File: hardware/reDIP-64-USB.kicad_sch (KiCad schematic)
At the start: 35 parts, among them J1 USB_C_Receptacle, Q1 PDTA143ZMB, U10 PTN5110, U11 FUSB340, U12 DSC1103CE2-135.0000, U13 FSA2259, U8 LFE5UM5G-25F-8MG285C

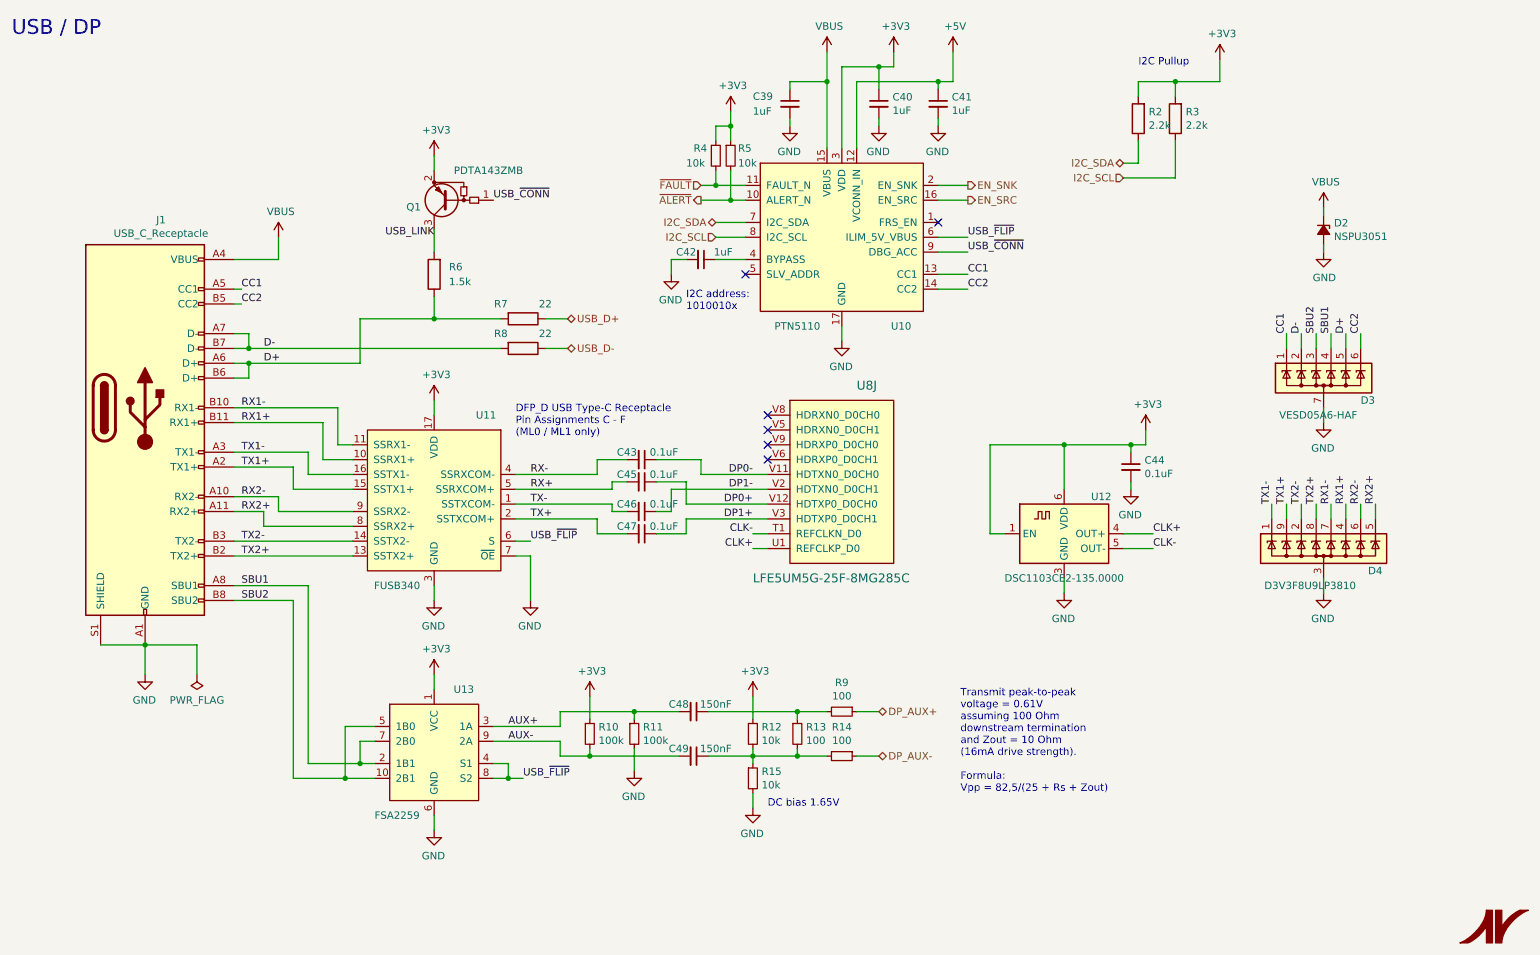
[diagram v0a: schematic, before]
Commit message: Various improvements
* Removed slash from sheet names
* Reannotated schematics
* Example derivation of clocks in schematics
* Identical capacitors for DisplayPort main lanes and AUX
* Replaced switch FSA2259UMX with FSUSB42UMX
* Modified PCB physical stackup to (hopefully) be manufacturable
* Only one microvia size (0.1mm)
* Changed track width for differential pairs
* Routing cleanups and improvements
* Added files for manufacture
* Updated README

Many thanks for advice and help go to @azonenberg, @DX-MON, @gatecat,
@smunaut, and @zyp.
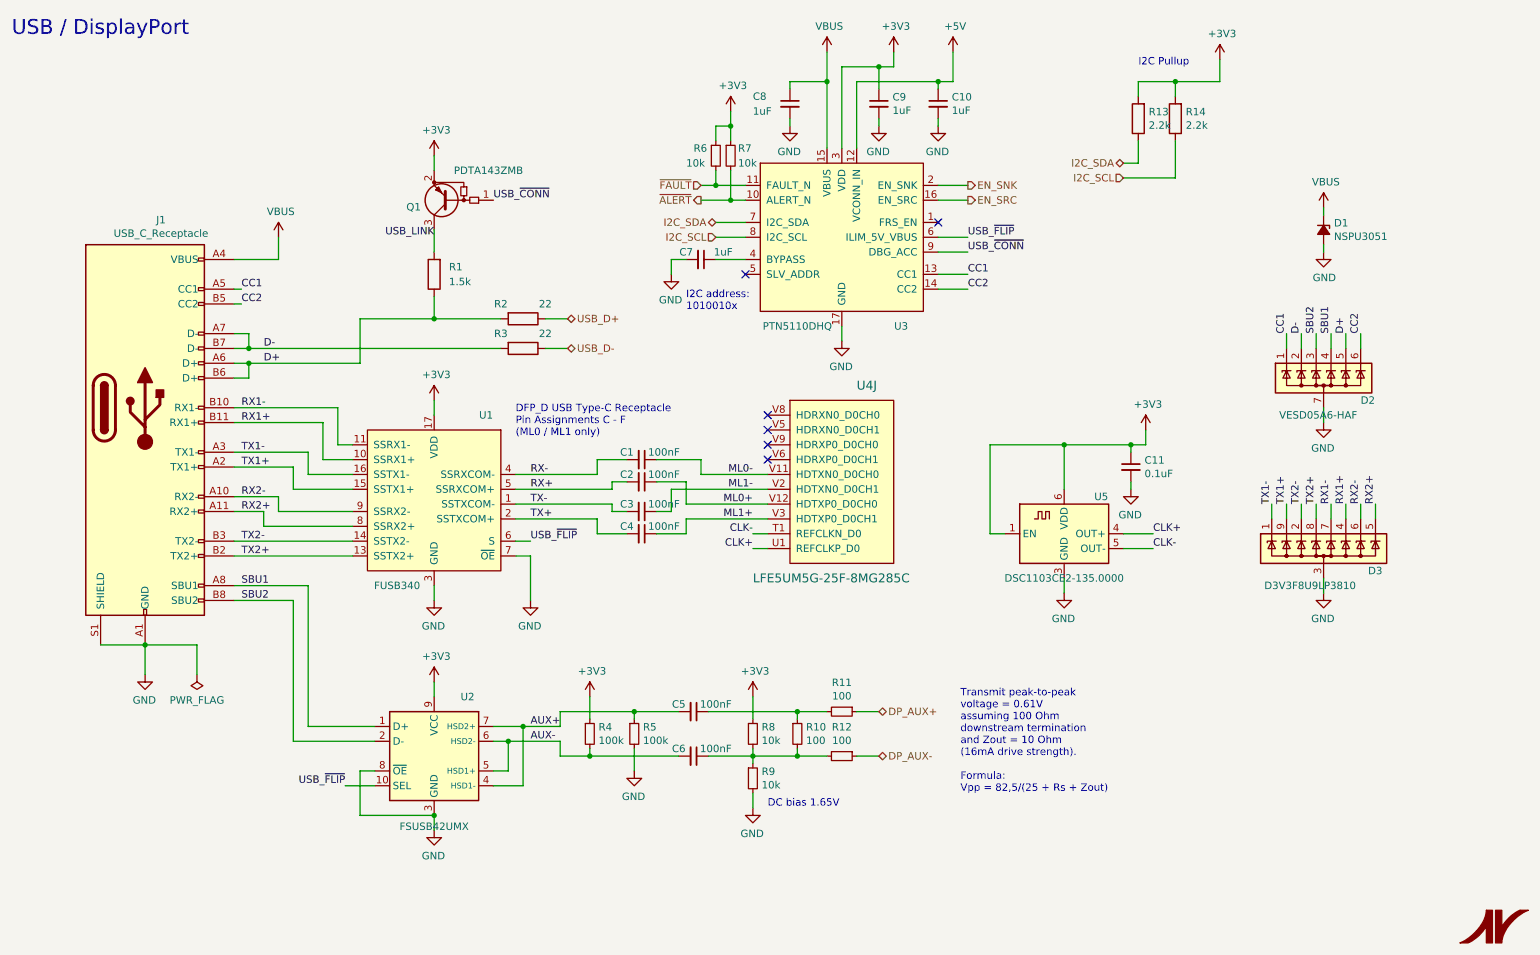
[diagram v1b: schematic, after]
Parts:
- removed U13: FSA2259, ONSemi:CASE523BC_1.4x1.8_P0.4mm, symbol ONSemi:FSA2259
- added U2: FSUSB42UMX, ONSemi:CASE523BC_1.4x1.8_P0.4mm, symbol ONSemi:FSUSB42UMX
- C1: renamed from C43; value 0.1uF -> 100nF; Notes 1.2V DC DERATED TO 0.1uF -> (none)
- C2: renamed from C45; value 0.1uF -> 100nF; Notes 1.2V DC DERATED TO 0.1uF -> (none)
- C3: renamed from C46; value 0.1uF -> 100nF; Notes 1.2V DC DERATED TO 0.1uF -> (none)
- C4: renamed from C47; value 0.1uF -> 100nF; Notes 1.2V DC DERATED TO 0.1uF -> (none)
- C5: renamed from C48; value 150nF -> 100nF; Notes 1.65V DC DERATED TO 150nF -> (none); PN GRM033R60J224ME15D -> GRM033R60J224KE15D
- C6: renamed from C49; value 150nF -> 100nF; Notes 1.65V DC DERATED TO 150nF -> (none); PN GRM033R60J224ME15D -> GRM033R60J224KE15D
- U3: renamed from U10; value PTN5110 -> PTN5110DHQ
- renumbered C41 to C10, C44 to C11, C42 to C7, C39 to C8, C40 to C9, D2 to D1, D3 to D2, D4 to D3, R6 to R1, R13 to R10, R9 to R11, R14 to R12, R2 to R13, R3 to R14, R7 to R2, R8 to R3, R10 to R4, R11 to R5, R4 to R6, R5 to R7, R12 to R8, R15 to R9, U11 to U1, U8 to U4, U12 to U5
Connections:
- net +3V3: now also U2.9 (VCC)
- net AUX+: now also U2.4 (HSD1-), U2.7 (HSD2+)
- net AUX-: now also U2.5 (HSD1+), U2.6 (HSD2-)
- net GND: now also U2.3 (GND), U2.8 (~OE)
- net SBU1: now also U2.1 (D+)
- net SBU2: now also U2.2 (D-)
- net USB_~FLIP~: now also U2.10 (SEL)
- net DP0+ renamed ML0+
- net DP0- renamed ML0-
- net DP1+ renamed ML1+
- net DP1- renamed ML1-
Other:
- note added: "USB / DisplayPort"
- note removed: "USB / DP"

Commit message: Corrected BOM for C1-C6
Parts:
- C1, C2, C3, C4, C5, C6: PN GRM033R60J224KE15D -> GRM033R60J104KE19D
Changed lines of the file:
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@@
       (effects (font (size 1.27 1.27)) hide)
     )
-    (property "PN" "GRM033R60J224KE15D" (id 6) (at 130.81 97.79 0)
+    (property "PN" "GRM033R60J104KE19D" (id 6) (at 130.81 97.79 0)
       (effects (font (size 1.27 1.27)) hide)
     )
@@
       (effects (font (size 1.27 1.27)) hide)
     )
-    (property "PN" "GRM033R60J224KE15D" (id 6) (at 130.81 101.6 0)
+    (property "PN" "GRM033R60J104KE19D" (id 6) (at 130.81 101.6 0)
       (effects (font (size 1.27 1.27)) hide)
     )
@@
       (effects (font (size 1.27 1.27)) hide)
     )
-    (property "PN" "GRM033R60J224KE15D" (id 6) (at 130.81 106.68 0)
+    (property "PN" "GRM033R60J104KE19D" (id 6) (at 130.81 106.68 0)
       (effects (font (size 1.27 1.27)) hide)
     )
@@
       (effects (font (size 1.27 1.27)) hide)
     )
-    (property "PN" "GRM033R60J224KE15D" (id 6) (at 130.81 110.49 0)
+    (property "PN" "GRM033R60J104KE19D" (id 6) (at 130.81 110.49 0)
       (effects (font (size 1.27 1.27)) hide)
     )
@@
       (effects (font (size 1.27 1.27)) hide)
     )
-    (property "PN" "GRM033R60J224KE15D" (id 7) (at 139.7 140.97 0)
+    (property "PN" "GRM033R60J104KE19D" (id 7) (at 139.7 140.97 0)
       (effects (font (size 1.27 1.27)) hide)
     )
@@
       (effects (font (size 1.27 1.27)) hide)
     )
-    (property "PN" "GRM033R60J224KE15D" (id 7) (at 139.7 148.59 0)
+    (property "PN" "GRM033R60J104KE19D" (id 7) (at 139.7 148.59 0)
       (effects (font (size 1.27 1.27)) hide)
     )

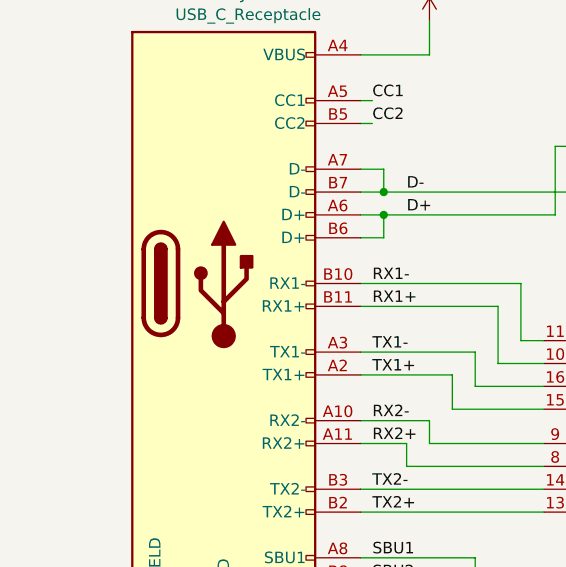
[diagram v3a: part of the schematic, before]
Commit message: Updated all KiCad files to current format
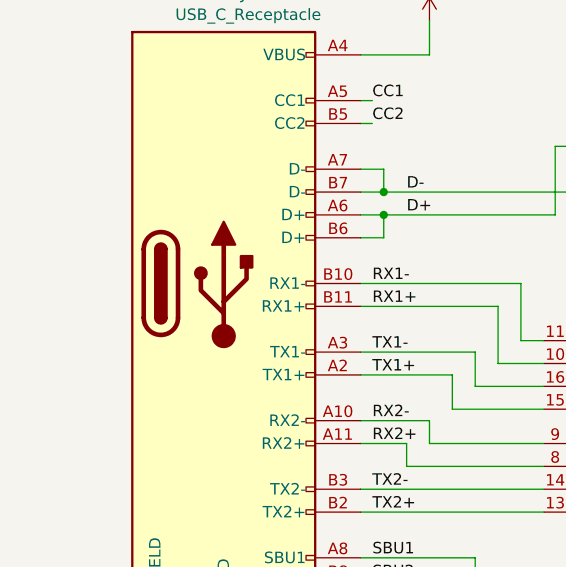
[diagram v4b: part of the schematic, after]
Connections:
- net USB_~CONN~ renamed USB_~{CONN}
- net USB_~FLIP~ renamed USB_~{FLIP}
- net ~ALERT~ renamed ~{ALERT}
- net ~FAULT~ renamed ~{FAULT}

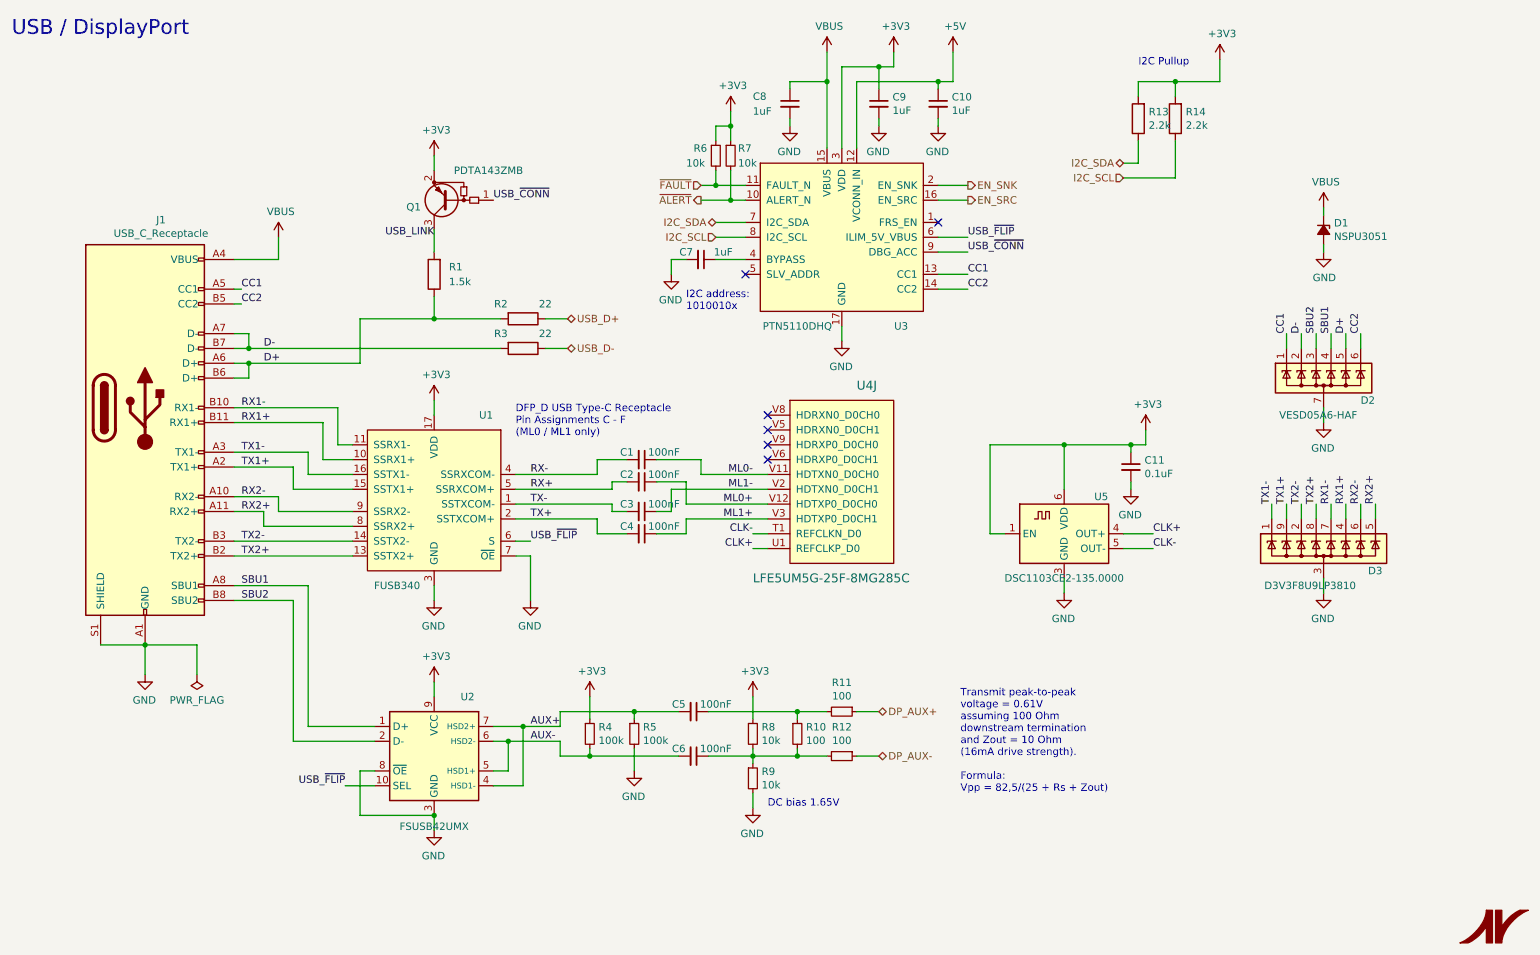
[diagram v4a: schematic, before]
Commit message: Revision 1.0
* USB receptacle replaced with GCT USB4080-03-A / HRO TYPE-C-31-M-05
* USB PD TCPC changed to PTN5110NHQ (FPF2286 has 15ms VBUS debounce time)
* Complete rework of power section
  - Over-voltage protection on VBUS (FPF2286 / FPF2495C)
  - Bidirectional VCC (2 x TPS22916)
  - Replaced EOLed buck converters with FAN53610 / FAN53611
  - Replaced EOLed LDO for ECP5 VCCAUX with NCP115AMX250TCG
  - Replaced LDO for SGTL5000 VDDA with 3.3V version
  - Added separate LDO for SGTL5000 VDDD, avoiding overvoltage on ECP5 VCC
* Bus switch changed to SN74CBT16211A, biased for level shifting
* Registered I/O for FLASH / HyperRAM clock
* Pin header changes:
  - Machined (round) pins for MOS6510 socket
  - Top only headers for additional I/O
  - Reworked pinout for VIC-II and SID
  - Removed 5V output (now available on bidirectional VCC)
  - Added GND for audio / 3.3V
  - Changed JTAG pinout to match Tag-Connect TC-LATTICE / TC-XILINX6
* Removed EXT_IN capacitors
* Button force changed from 240gf to 100gf
* Space for UL and date codes
* Black solder mask
* Silk screen updates
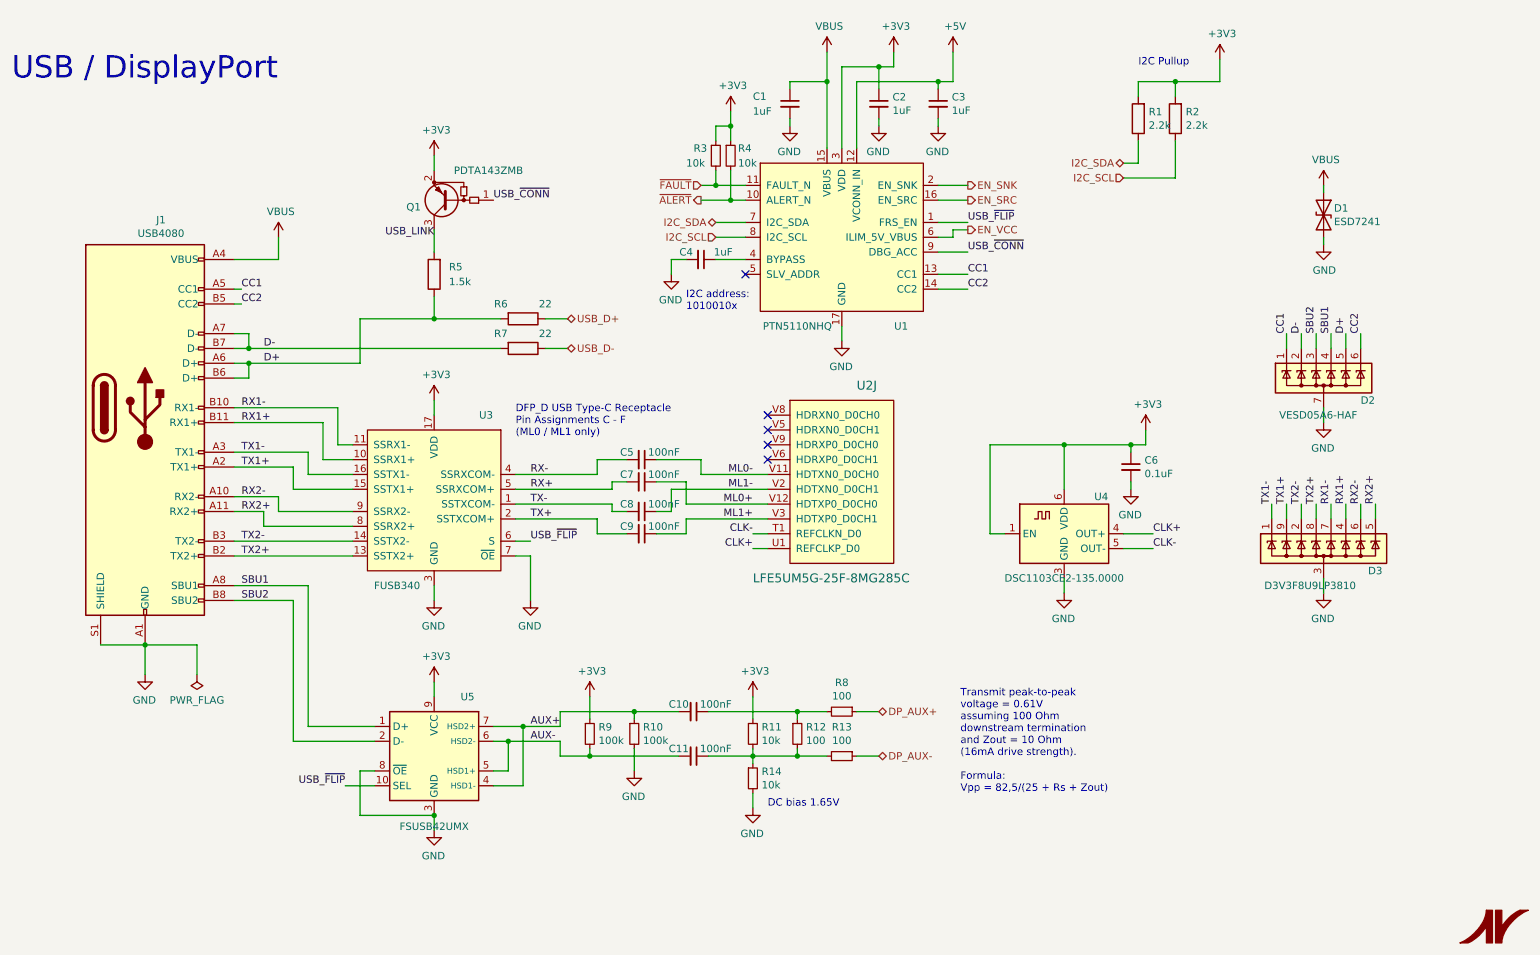
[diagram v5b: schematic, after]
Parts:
- D1: value NSPU3051 -> ESD7241; footprint ONSemi:CASE714AB_1.0x0.6mm -> ONSemi:CASE_714AB_1.0x0.6mm; symbol Device:D_Zener_Small_Filled -> Device:D_TVS; Mfg ON Semiconductor -> onsemi; PN NSPU3051N2T5G -> ESD7241N2T5G
- J1: value USB_C_Receptacle -> USB4080; footprint JAE:USB_C_Receptacle_JAE_DX07S024JA1 -> GCT:USB_C_Receptacle_GCT_USB4080; Mfg JAE -> GCT; Notes (none) -> REPLACEMENT PART: HRO TYPE-C-31-M-05; PN DX07S024JA1R1300 -> USB4080-03-A
- R1: renamed from R13; PN ERJ-1GNJ222C -> ERJ1GNJ222C
- R10: renamed from R5; PN ERJ-1GNJ104C -> ERJ1GNJ104C
- R11: renamed from R8; PN ERJ-1GNJ103C -> ERJ1GNJ103C
- R12: renamed from R10; PN ERJ-1GNF1000C -> ERJ1GNF1000C
- R13: renamed from R12; PN ERJ-1GNF1000C -> ERJ1GNF1000C
- R14: renamed from R9; PN ERJ-1GNJ103C -> ERJ1GNJ103C
- R2: renamed from R14; PN ERJ-1GNJ222C -> ERJ1GNJ222C
- R3: renamed from R6; PN ERJ-1GNJ103C -> ERJ1GNJ103C
- R4: renamed from R7; PN ERJ-1GNJ103C -> ERJ1GNJ103C
- R5: renamed from R1; PN ERJ-1GNJ152C -> ERJ1GNJ152C
- R6: renamed from R2; PN ERJ-1GNJ220C -> ERJ1GNJ220C
- R7: renamed from R3; PN ERJ-1GNJ220C -> ERJ1GNJ220C
- R8: renamed from R11; PN ERJ-1GNF1000C -> ERJ1GNF1000C
- R9: renamed from R4; PN ERJ-1GNJ104C -> ERJ1GNJ104C
- U1: renamed from U3; value PTN5110DHQ -> PTN5110NHQ; PN PTN5110DHQZ -> PTN5110NHQZ
- U3: renamed from U1; footprint ONSemi:CASE722AB_2.0x2.8mm_P0.4mm -> ONSemi:CASE_722AB_2.0x2.8mm_P0.4mm; Mfg ON Semiconductor -> onsemi
- U5: renamed from U2; footprint ONSemi:CASE523BC_1.4x1.8_P0.4mm -> ONSemi:CASE_523BC_1.4x1.8_P0.4mm; Mfg ON Semiconductor -> onsemi
- renumbered C8 to C1, C5 to C10, C6 to C11, C9 to C2, C10 to C3, C7 to C4, C1 to C5, C11 to C6, C2 to C7, C3 to C8, C4 to C9, U4 to U2, U5 to U4
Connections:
- net USB_~{FLIP}: now also U1.1 (FRS_EN); no longer U1.6 (ILIM_5V_VBUS)
- new net EN_VCC: U1.6 (ILIM_5V_VBUS)
- no-connect marks 6 -> 5
